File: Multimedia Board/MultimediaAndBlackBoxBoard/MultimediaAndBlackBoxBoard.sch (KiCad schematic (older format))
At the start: 19 parts

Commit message: Multimedia and Black Box Board finished
real time clock added, sd card circuit fixed, indicators for all pins added (blue bc pink out of stock everywhere), etc
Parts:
- removed C? (x2): 1000uF, symbol Device:C
- removed C? (x2): 100uF, symbol Device:C
- removed D?: Green LED, symbol Device:LED
- removed D? (x2): D_Schottky, symbol Device:D_Schottky
- removed D?: LED, symbol Device:LED
- removed J?: Test_Point, symbol Connector:TestPoint
- removed J?: Test_Point, symbol MRDT_Connectors:Test_Point
- removed L?: 100uH, symbol Device:L
- removed L?: L, symbol Device:L
- removed R?: 330, symbol Device:R
- removed R?: 500, symbol Device:R
- removed U?: LM2576D2TR4, symbol MRDT_Devices:LM2576D2TR4
- removed U?: LM2576SX-5, symbol MRDT_Devices:LM2576D2TR4
- added C1, C2, C3, C4: 10uF, symbol Device:C_Small
- added D? (x6): BLUE, symbol Device:LED_Small
- added D? (x2): GREEN, symbol Device:LED_Small
- added R? (x7): 480, symbol Device:R_Small
- added R?: 330, symbol Device:R_Small
- added U1, U2: OKI, symbol MRDT_Devices:OKI
- Conn1: renamed from Conn?; value AndersonPP -> Multimedia
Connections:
- net labels added: +12V, +12VA, SCL, SDA, SD_CD, SD_RX, SD_Select, SD_TX
- net labels removed: 12V_Logic, 12_Actuation
- wire segments 63 -> 62
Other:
- moved on the sheet: Conn1A, Conn1B, Conn1C

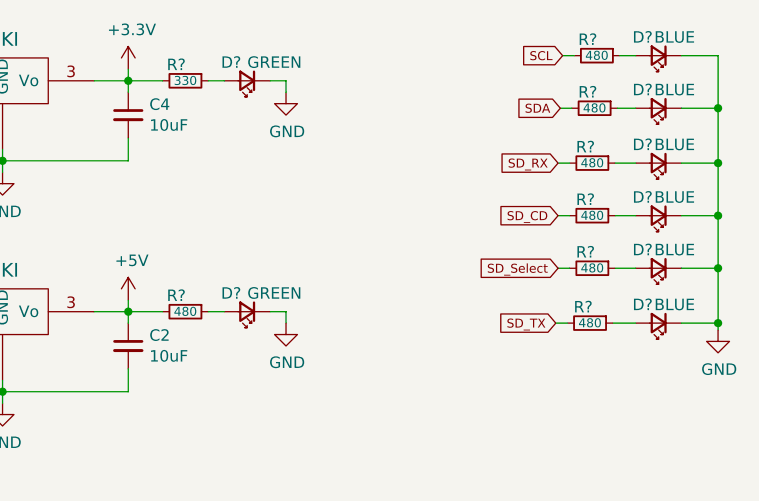
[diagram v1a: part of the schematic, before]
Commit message: layout started
most components placed, battery cell wont cooperate (nets arent right)
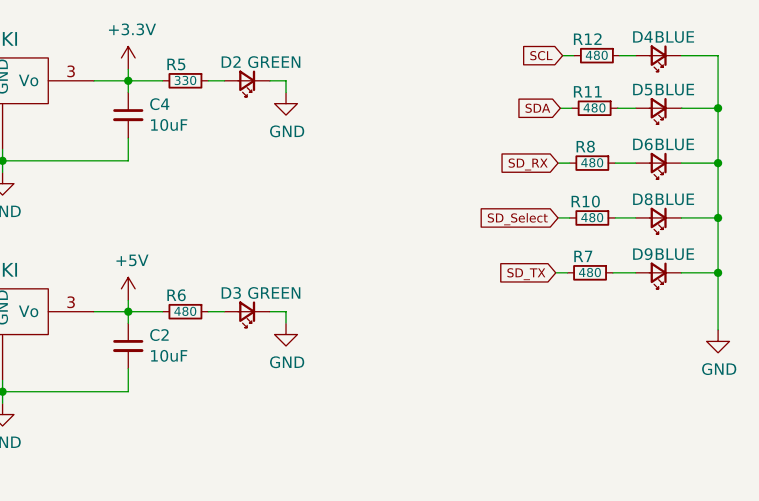
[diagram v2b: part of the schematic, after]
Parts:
- removed D?: BLUE, symbol Device:LED_Small
- removed R?: 480, symbol Device:R_Small
- C1, C2, C3, C4: footprint (none) -> Capacitor_SMD:C_0603_1608Metric_Pad1.05x0.95mm_HandSolder
- Conn1: footprint (none) -> MRDT_Connectors:Anderson_3_Horizontal_Side_by_Side
- D2, D3, D4, D5, D6, D8, D9: renamed from D?; footprint (none) -> LED_SMD:LED_0603_1608Metric_Pad1.05x0.95mm_HandSolder
- R10, R11, R12, R5, R6, R7, R8: renamed from R?; footprint (none) -> Resistor_SMD:R_0603_1608Metric_Pad1.05x0.95mm_HandSolder
- U1, U2: footprint (none) -> MRDT_Devices:OKI_Horizontal
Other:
- moved on the sheet: D8, D9, R10, R7

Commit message: Finished Board
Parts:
- removed D8: BLUE, LED_SMD:LED_0603_1608Metric_Pad1.05x0.95mm_HandSolder, symbol Device:LED_Small
- removed R10: 480, Resistor_SMD:R_0603_1608Metric_Pad1.05x0.95mm_HandSolder, symbol Device:R_Small
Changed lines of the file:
@@
 	8290 860  8440 860
 Wire Wire Line
-	10870 1220 10870 1460
-Wire Wire Line
-	10710 1460 10870 1460
-Wire Wire Line
 	10410 1700 10510 1700
-Wire Wire Line
-	10420 1460 10510 1460
-$Comp
-L Device:LED_Small D8
-U 1 1 5FD1E83A
-P 10610 1460
-F 0 "D8" H 10680 1380 50  0000 C CNN
-F 1 "BLUE" H 10540 1380 50  0000 C CNN
-F 2 "LED_SMD:LED_0603_1608Metric_Pad1.05x0.95mm_HandSolder" V 10610 1460 50  0001 C CNN
-F 3 "~" V 10610 1460 50  0001 C CNN
-	1    10610 1460
-	-1   0    0    1
-$EndComp
 $Comp
 L Device:LED_Small D9
@@
 Wire Wire Line
 	10160 1700 10210 1700
-Wire Wire Line
-	10170 1460 10220 1460
 $Comp
 L Device:R_Small R7
@@
 	0    1    1    0
 $EndComp
-$Comp
-L Device:R_Small R10
-U 1 1 5FCF4A7B
-P 10320 1460
-F 0 "R10" V 10250 1430 50  0000 C CNN
-F 1 "480" V 10320 1460 39  0000 C CNN
-F 2 "Resistor_SMD:R_0603_1608Metric_Pad1.05x0.95mm_HandSolder" H 10320 1460 50  0001 C CNN
-F 3 "~" H 10320 1460 50  0001 C CNN
-	1    10320 1460
-	0    1    1    0
-$EndComp
-Text GLabel 10170 1460 0    39   Input ~ 0
-SD_Select
 Text GLabel 10160 1700 0    39   Input ~ 0
 SD_TX
-Connection ~ 10870 1460
-Wire Wire Line
-	10870 1460 10870 1700
 Wire Wire Line
 	10710 1700 10870 1700
@@
 Wire Wire Line
 	10870 1700 10870 1950
+Wire Wire Line
+	10870 1220 10870 1700
 $EndSCHEMATC

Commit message: SCLK added for SPI, tags renamed appropriately
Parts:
- added D7: BLUE, LED_SMD:LED_0603_1608Metric_Pad1.05x0.95mm_HandSolder, symbol Device:LED_Small
- added R9: 330, Resistor_SMD:R_0603_1608Metric_Pad0.98x0.95mm_HandSolder, symbol Device:R_Small
- C1, C2, C3, C4: footprint Capacitor_SMD:C_0603_1608Metric_Pad1.05x0.95mm_HandSolder -> Capacitor_SMD:C_0603_1608Metric_Pad1.08x0.95mm_HandSolder
- R11, R12, R5, R6: footprint Resistor_SMD:R_0603_1608Metric_Pad1.05x0.95mm_HandSolder -> Resistor_SMD:R_0603_1608Metric_Pad0.98x0.95mm_HandSolder
- R7, R8: value 480 -> 330; footprint Resistor_SMD:R_0603_1608Metric_Pad1.05x0.95mm_HandSolder -> Resistor_SMD:R_0603_1608Metric_Pad0.98x0.95mm_HandSolder
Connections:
- net GND: now also D7.1 (K)
- net SD_RX renamed SD_MISO
- net SD_TX renamed SD_MOSI
- new net: D7.2 (A), R9.1
- new net SD_SCLK: R9.2
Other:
- moved on the sheet: D9, R7
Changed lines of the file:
@@
 F 0 "C1" H 7282 2066 50  0000 L CNN
 F 1 "10uF" H 7282 1975 50  0000 L CNN
-F 2 "Capacitor_SMD:C_0603_1608Metric_Pad1.05x0.95mm_HandSolder" H 7190 2020 50  0001 C CNN
+F 2 "Capacitor_SMD:C_0603_1608Metric_Pad1.08x0.95mm_HandSolder" H 7190 2020 50  0001 C CNN
 F 3 "~" H 7190 2020 50  0001 C CNN
 	1    7190 2020
@@
 F 0 "C2" H 8382 2066 50  0000 L CNN
 F 1 "10uF" H 8382 1975 50  0000 L CNN
-F 2 "Capacitor_SMD:C_0603_1608Metric_Pad1.05x0.95mm_HandSolder" H 8290 2020 50  0001 C CNN
+F 2 "Capacitor_SMD:C_0603_1608Metric_Pad1.08x0.95mm_HandSolder" H 8290 2020 50  0001 C CNN
 F 3 "~" H 8290 2020 50  0001 C CNN
 	1    8290 2020
@@
 F 0 "C3" H 7282 1056 50  0000 L CNN
 F 1 "10uF" H 7282 965 50  0000 L CNN
-F 2 "Capacitor_SMD:C_0603_1608Metric_Pad1.05x0.95mm_HandSolder" H 7190 1010 50  0001 C CNN
+F 2 "Capacitor_SMD:C_0603_1608Metric_Pad1.08x0.95mm_HandSolder" H 7190 1010 50  0001 C CNN
 F 3 "~" H 7190 1010 50  0001 C CNN
 	1    7190 1010
@@
 F 0 "C4" H 8382 1056 50  0000 L CNN
 F 1 "10uF" H 8382 965 50  0000 L CNN
-F 2 "Capacitor_SMD:C_0603_1608Metric_Pad1.05x0.95mm_HandSolder" H 8290 1010 50  0001 C CNN
+F 2 "Capacitor_SMD:C_0603_1608Metric_Pad1.08x0.95mm_HandSolder" H 8290 1010 50  0001 C CNN
 F 3 "~" H 8290 1010 50  0001 C CNN
 	1    8290 1010
@@
 $EndComp
 Text GLabel 10170 1220 0    39   Input ~ 0
-SD_RX
+SD_MISO
 Text GLabel 10190 750  0    39   Input ~ 0
 SCL
@@
 F 0 "R12" V 10270 710 50  0000 C CNN
 F 1 "480" V 10340 750 39  0000 C CNN
-F 2 "Resistor_SMD:R_0603_1608Metric_Pad1.05x0.95mm_HandSolder" H 10340 750 50  0001 C CNN
+F 2 "Resistor_SMD:R_0603_1608Metric_Pad0.98x0.95mm_HandSolder" H 10340 750 50  0001 C CNN
 F 3 "~" H 10340 750 50  0001 C CNN
 	1    10340 750
@@
 F 0 "R11" V 10260 950 50  0000 C CNN
 F 1 "480" V 10330 980 39  0000 C CNN
-F 2 "Resistor_SMD:R_0603_1608Metric_Pad1.05x0.95mm_HandSolder" H 10330 980 50  0001 C CNN
+F 2 "Resistor_SMD:R_0603_1608Metric_Pad0.98x0.95mm_HandSolder" H 10330 980 50  0001 C CNN
 F 3 "~" H 10330 980 50  0001 C CNN
 	1    10330 980
@@
 P 10320 1220
 F 0 "R8" V 10250 1190 50  0000 C CNN
-F 1 "480" V 10320 1220 39  0000 C CNN
-F 2 "Resistor_SMD:R_0603_1608Metric_Pad1.05x0.95mm_HandSolder" H 10320 1220 50  0001 C CNN
+F 1 "330" V 10320 1220 39  0000 C CNN
+F 2 "Resistor_SMD:R_0603_1608Metric_Pad0.98x0.95mm_HandSolder" H 10320 1220 50  0001 C CNN
 F 3 "~" H 10320 1220 50  0001 C CNN
 	1    10320 1220
@@
 L power:GND #PWR03
 U 1 1 5FD2B619
-P 10870 1950
-F 0 "#PWR03" H 10870 1700 50  0001 C CNN
-F 1 "GND" H 10875 1777 50  0000 C CNN
-F 2 "" H 10870 1950 50  0001 C CNN
-F 3 "" H 10870 1950 50  0001 C CNN
-	1    10870 1950
+P 10870 1800
+F 0 "#PWR03" H 10870 1550 50  0001 C CNN
+F 1 "GND" H 10875 1627 50  0000 C CNN
+F 2 "" H 10870 1800 50  0001 C CNN
+F 3 "" H 10870 1800 50  0001 C CNN
+	1    10870 1800
 	1    0    0    -1
 $EndComp
@@
 F 0 "R5" V 8470 820 50  0000 C CNN
 F 1 "330" V 8540 860 39  0000 C CNN
-F 2 "Resistor_SMD:R_0603_1608Metric_Pad1.05x0.95mm_HandSolder" H 8540 860 50  0001 C CNN
+F 2 "Resistor_SMD:R_0603_1608Metric_Pad0.98x0.95mm_HandSolder" H 8540 860 50  0001 C CNN
 F 3 "~" H 8540 860 50  0001 C CNN
 	1    8540 860
@@
 F 0 "R6" V 8470 1830 50  0000 C CNN
 F 1 "480" V 8540 1870 39  0000 C CNN
-F 2 "Resistor_SMD:R_0603_1608Metric_Pad1.05x0.95mm_HandSolder" H 8540 1870 50  0001 C CNN
+F 2 "Resistor_SMD:R_0603_1608Metric_Pad0.98x0.95mm_HandSolder" H 8540 1870 50  0001 C CNN
 F 3 "~" H 8540 1870 50  0001 C CNN
 	1    8540 1870
@@
 	8290 860  8440 860
 Wire Wire Line
-	10410 1700 10510 1700
+	10160 1470 10210 1470
+Text GLabel 10160 1470 0    50   Input ~ 0
+SD_MOSI
+Text GLabel 10160 1690 0    50   Input ~ 0
+SD_SCLK
+Wire Wire Line
+	10410 1470 10510 1470
 $Comp
 L Device:LED_Small D9
 U 1 1 5FD1E834
-P 10610 1700
-F 0 "D9" H 10680 1620 50  0000 C CNN
-F 1 "BLUE" H 10540 1620 50  0000 C CNN
-F 2 "LED_SMD:LED_0603_1608Metric_Pad1.05x0.95mm_HandSolder" V 10610 1700 50  0001 C CNN
-F 3 "~" V 10610 1700 50  0001 C CNN
-	1    10610 1700
-	-1   0    0    1
-$EndComp
-Wire Wire Line
-	10160 1700 10210 1700
+P 10610 1470
+F 0 "D9" H 10680 1390 50  0000 C CNN
+F 1 "BLUE" H 10540 1390 50  0000 C CNN
+F 2 "LED_SMD:LED_0603_1608Metric_Pad1.05x0.95mm_HandSolder" V 10610 1470 50  0001 C CNN
+F 3 "~" V 10610 1470 50  0001 C CNN
+	1    10610 1470
+	-1   0    0    1
+$EndComp
 $Comp
 L Device:R_Small R7
 U 1 1 5FCF4A81
-P 10310 1700
-F 0 "R7" V 10240 1670 50  0000 C CNN
-F 1 "480" V 10310 1700 39  0000 C CNN
-F 2 "Resistor_SMD:R_0603_1608Metric_Pad1.05x0.95mm_HandSolder" H 10310 1700 50  0001 C CNN
-F 3 "~" H 10310 1700 50  0001 C CNN
-	1    10310 1700
-	0    1    1    0
-$EndComp
-Text GLabel 10160 1700 0    39   Input ~ 0
-SD_TX
-Wire Wire Line
-	10710 1700 10870 1700
-Connection ~ 10870 1700
-Wire Wire Line
-	10870 1700 10870 1950
-Wire Wire Line
-	10870 1220 10870 1700
+P 10310 1470
+F 0 "R7" V 10240 1440 50  0000 C CNN
+F 1 "330" V 10310 1470 39  0000 C CNN
+F 2 "Resistor_SMD:R_0603_1608Metric_Pad0.98x0.95mm_HandSolder" H 10310 1470 50  0001 C CNN
+F 3 "~" H 10310 1470 50  0001 C CNN
+	1    10310 1470
+	0    1    1    0
+$EndComp
+Wire Wire Line
+	10870 1220 10870 1470
+Connection ~ 10870 1470
+Wire Wire Line
+	10710 1470 10870 1470
+Wire Wire Line
+	10410 1690 10510 1690
+$Comp
+L Device:LED_Small D7
+U 1 1 5FC96A61
+P 10610 1690
+F 0 "D7" H 10680 1610 50  0000 C CNN
+F 1 "BLUE" H 10540 1610 50  0000 C CNN
+F 2 "LED_SMD:LED_0603_1608Metric_Pad1.05x0.95mm_HandSolder" V 10610 1690 50  0001 C CNN
+F 3 "~" V 10610 1690 50  0001 C CNN
+	1    10610 1690
+	-1   0    0    1
+$EndComp
+$Comp
+L Device:R_Small R9
+U 1 1 5FC96A67
+P 10310 1690
+F 0 "R9" V 10240 1660 50  0000 C CNN
+F 1 "330" V 10310 1690 39  0000 C CNN
+F 2 "Resistor_SMD:R_0603_1608Metric_Pad0.98x0.95mm_HandSolder" H 10310 1690 50  0001 C CNN
+F 3 "~" H 10310 1690 50  0001 C CNN
+	1    10310 1690
+	0    1    1    0
+$EndComp
+Wire Wire Line
+	10710 1690 10870 1690
+Wire Wire Line
+	10210 1690 10160 1690
+Wire Wire Line
+	10870 1470 10870 1690
+Connection ~ 10870 1690
+Wire Wire Line
+	10870 1690 10870 1800
 $EndSCHEMATC
